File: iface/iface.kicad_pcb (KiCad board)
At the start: 2 copper layers, 215.9 x 152.4 mm, 157 parts, among them J1 Barrel_Jack_Switch, J10 4P4C, J11 4P4C, J12 4P4C, J2 Conn_01x16, J3 4P4C, J4 4P4C, J5 4P4C, J6 4P4C, J7 4P4C, J8 4P4C, J9 4P4C, Q1 BC847, Q10 BC847, Q11 BC847, Q12 BC847, Q13 BC847, Q14 BC847, Q15 BC847, Q16 BC847, Q17 BC847, Q18 BC847, Q19 BC847, Q2 BC847, Q20 BC847, Q21 BC847, Q22 BC847, Q23 BC847, Q24 BC847, Q25 BC847, Q26 BC847, Q27 BC847, Q28 BC847, Q29 BC847, Q3 BC847, Q30 BC847, Q31 BC847, Q32 BC847, Q33 BC847, Q34 BC847, Q35 BC847, Q36 BC847, Q37 BC847, Q38 BC847, Q39 BC847, Q4 BC847, Q40 BC847, Q5 BC847, Q6 BC847, Q7 BC847, Q8 BC847, Q9 BC847, SW1 SW_DPDT_x2, U1 74HC595, U10 PC817, U11 PC817, U12 PC817, U13 PC817, U14 PC817, U15 PC817, U16 PC817, U17 PC817, U18 PC817, U19 PC817, U2 74HC595, U20 PC817, U21 PC817, U22 PC817, U23 PC817, U24 PC817, U3 74HC04, U4 74HC04, U5 PC817, U6 PC817, U7 PC817, U8 PC817, U9 PC817

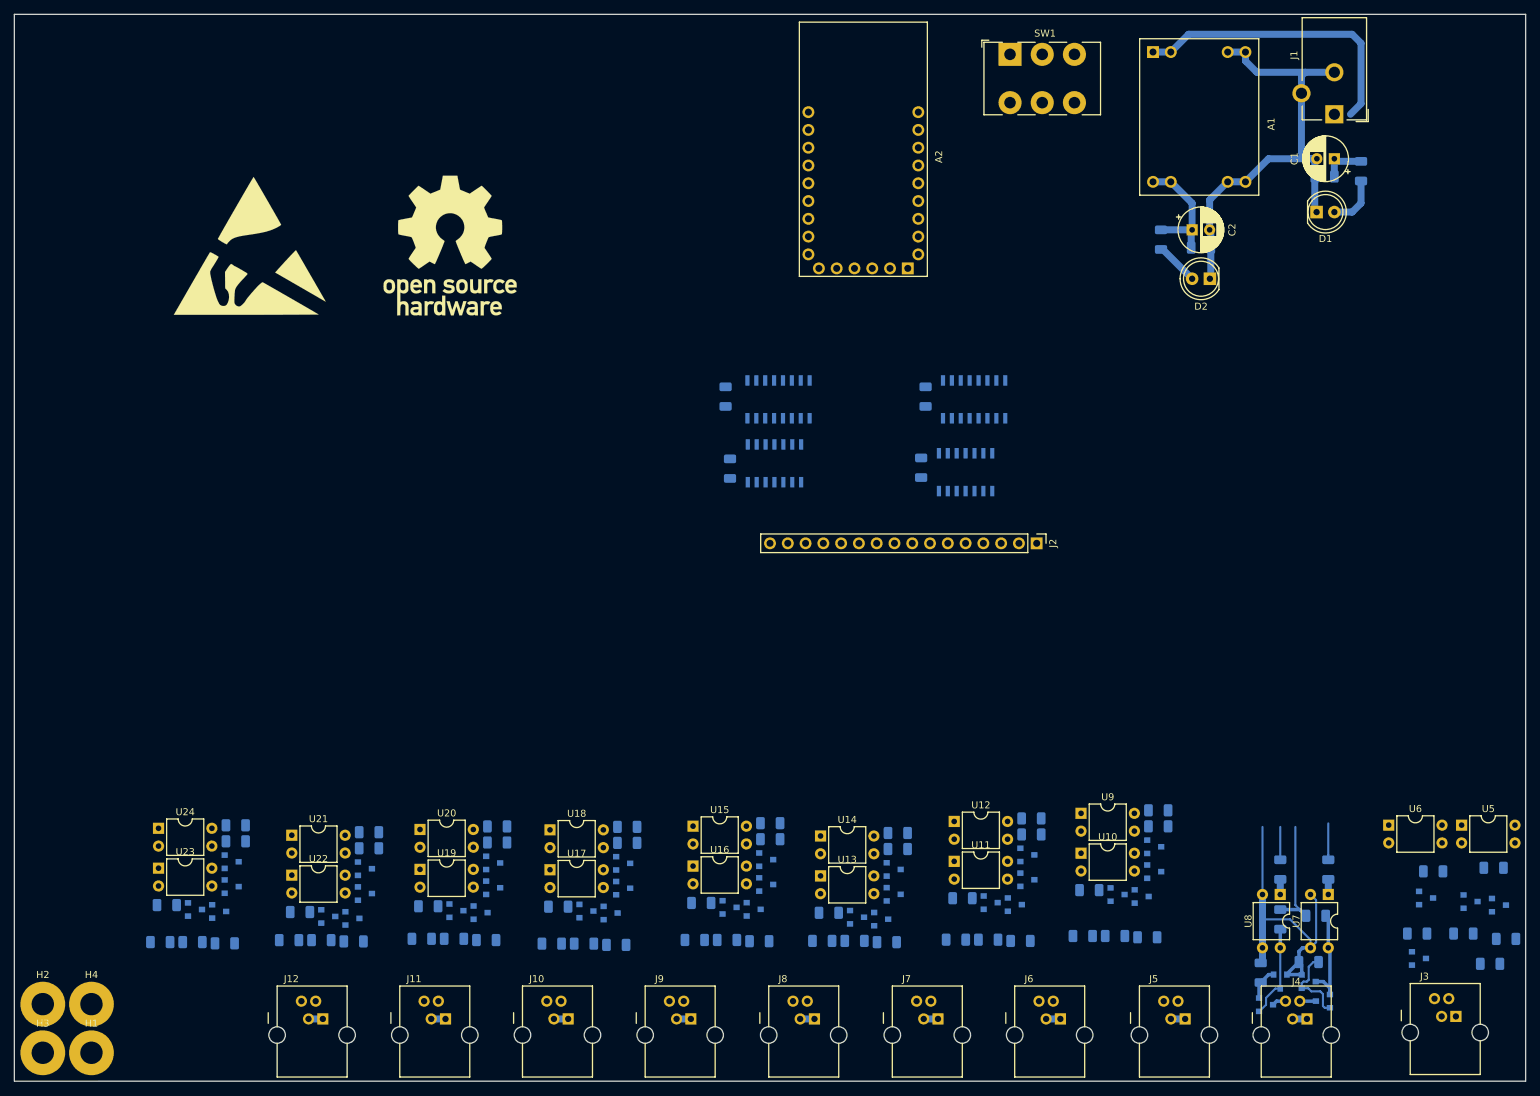
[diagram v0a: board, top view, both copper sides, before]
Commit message: iface: Finish routing the PCB layout
Signed-off-by: Sam Protsenko <joe.skb7@gmail.com>
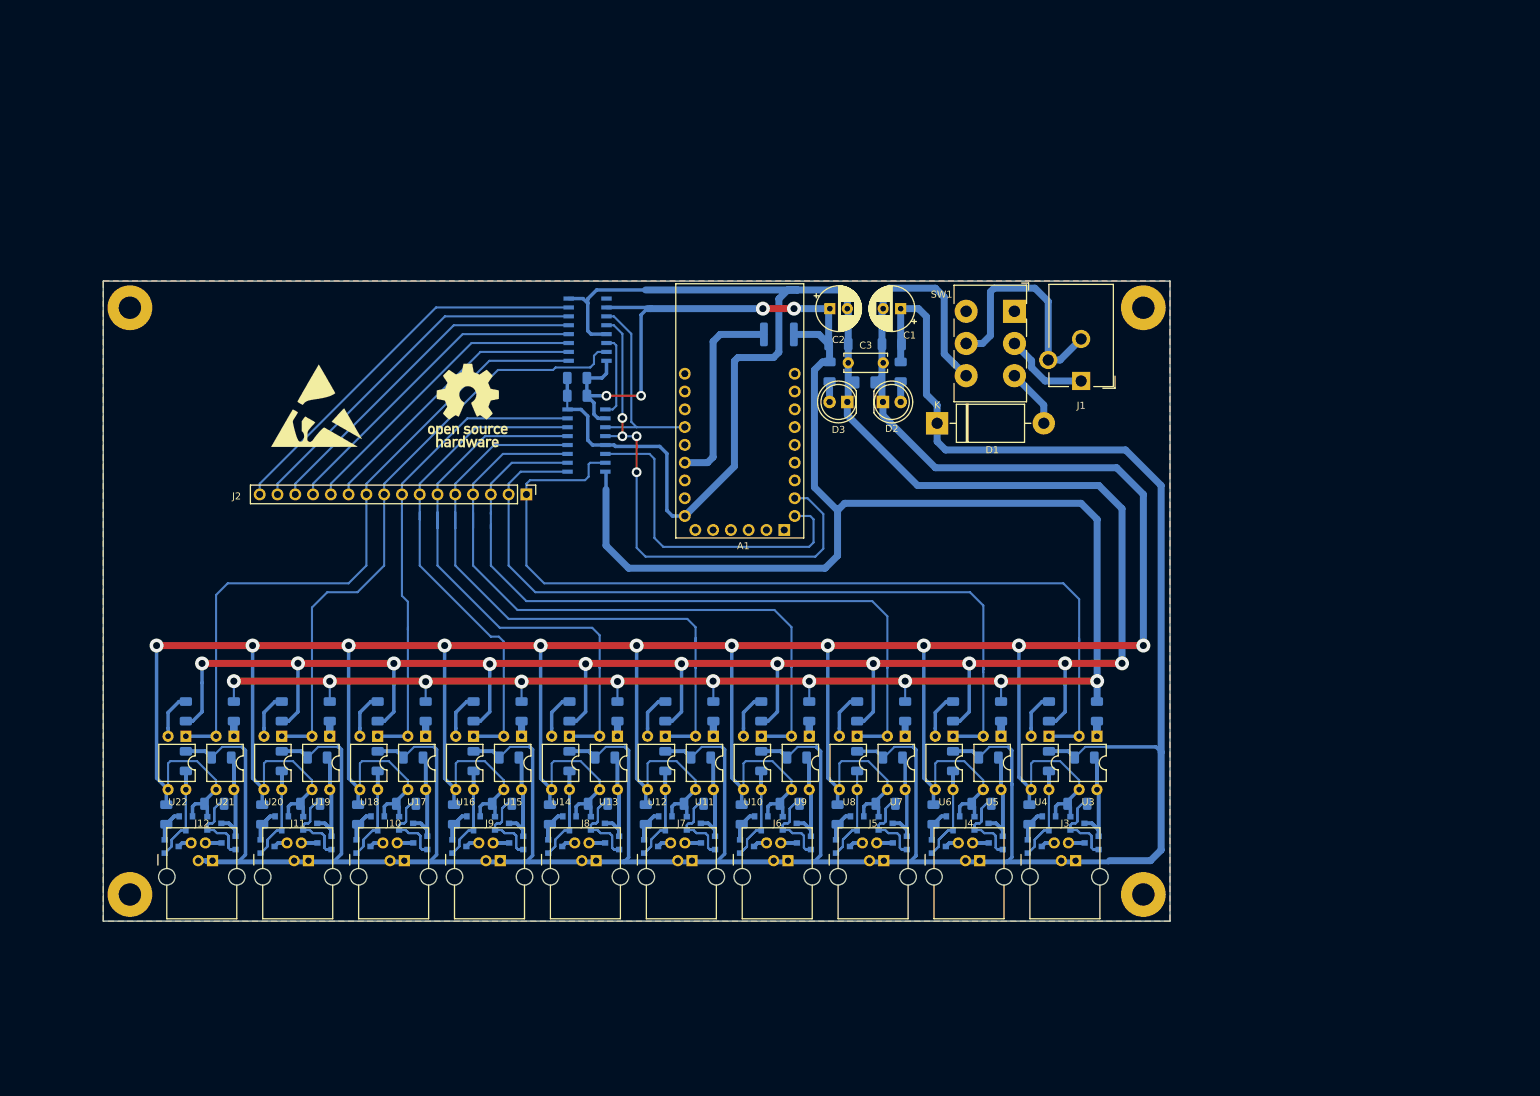
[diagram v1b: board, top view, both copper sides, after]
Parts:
- removed A2: FTDI232, Module_FTDI232:FTDI232
- removed the C4 at (233.0, 46.0)
- removed the C7 at (193.0, 77.5)
- removed C8: 100n, Capacitor_SMD:C_1206_3216Metric
- removed the D2 at (234.3, 50.5)
- removed U23, U24: PC817, Package_DIP:DIP-4_W7.62mm
- added C3: 1nF/2kV, Capacitor_THT:C_Disc_D6.0mm_W2.5mm_P5.00mm, F.Cu at (182.6, 62.5)
- added C6: 100nF, Capacitor_SMD:C_1206_3216Metric, B.Cu at (143.9, 64.6)
- added D1: 1N5822, Diode_THT:D_DO-201AD_P15.24mm_Horizontal, F.Cu at (195.3, 71.1)
- added D3: RED, LED_THT:LED_D5.0mm, F.Cu at (182.5, 68.1)
- added F1: Polyfuse, Fuse:Fuse_1812_4532Metric, B.Cu at (172.7, 58.4)
- added R63: 39R, Resistor_SMD:R_1206_3216Metric, B.Cu at (85.2, 127.0)
- A1: value MP1584_D-SUN -> FTDI232; footprint Module_MP1584:MP1584_D-SUN -> Module_FTDI232:FTDI232
- C1, C2: value 100uF x 25V -> 100uF/25V
- C4: renamed from C3; value 100n -> 100nF
- C5: value 100n -> 100nF
- C7: renamed from C6; value 100n -> 100nF
- R1: value 820R -> 1M
- R11, R17, R23, R29, R35, R41, R47, R5, R53, R59: value 10k -> 470R
- R13, R19, R25, R31, R37, R43, R49, R55, R61, R7: value 39R -> 10k
- R15, R21, R27, R33, R39, R45, R51, R57, R9: value 470R -> 39R
- R2: value 330R -> 820R
- R3: value 470R -> 330R
- SYM1: footprint Symbol:ESD-Logo_22x20mm_SilkScreen -> Symbol:ESD-Logo_13.2x12mm_SilkScreen
- SYM2: footprint Symbol:OSHW-Logo_19x20mm_SilkScreen -> Symbol:OSHW-Logo_11.4x12mm_SilkScreen
- U3, U4: value 74HC04 -> PC817; footprint Package_SO:SOIC-14_3.9x8.7mm_P1.27mm -> Package_DIP:DIP-4_W7.62mm; moved to F.Cu
- moved H2 186.1 mm to (224.8, 54.6)
- moved H3 158.8 mm to (224.8, 138.4)
- moved R3 126.1 mm to (180.0, 63.8), turned to 90 degrees
- moved H1 106.6 mm to (80.0, 54.6)
- moved A1 94.9 mm to (173.5, 86.4)
- moved R1 77.0 mm to (185.0, 65.3), turned to 0 degrees
- moved J2 73.2 mm to (136.7, 81.3)
- moved D2 67.6 mm to (187.6, 68.1)
- moved U5 67.0 mm to (204.5, 115.8), turned to 270 degrees
- moved C4 66.3 mm to (188.8, 59.8)
- moved C1 65.6 mm to (190.1, 54.7)
- moved Q2 65.3 mm to (211.3, 128.3), turned to 270 degrees
- moved R6 65.0 mm to (216.4, 118.9)
- moved U8 64.5 mm to (183.9, 115.8)
- moved U7 64.5 mm to (190.8, 115.8)
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- renumbered D1 to D2
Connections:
- net /Logic/G10 renamed /Logic/D10
- net /Logic/G11 renamed /Logic/D11
- net /Logic/G12 renamed /Logic/D12
- net /Logic/G13 renamed /Logic/D13
- net /Logic/G14 renamed /Logic/D14
- net /Logic/G15 renamed /Logic/D15
- A1 pad 1: +12V -> (no net)
- A1 pad 2: +12V -> (no net)
- A1 pad 3: GND -> (no net)
- A1 pad 4: GND -> (no net)
- A1 pad 5: +5V -> (no net)
- A1 pad 6: +5V -> (no net)
- A1 pad 7: GND -> GNDD
- A1 pad 8: GND -> (no net)
- C1 pad 2: GND -> GNDPWR
- C2 pad 2: GND -> GNDD
- C4 pad 2: GND -> GNDPWR
- C5 pad 2: GND -> GNDD
- C7 pad 2: GND -> GNDD
- D2 pad 1: GND -> GNDPWR
- D2 pad 2: Net-(D1-Pad2) -> Net-(D2-Pad2)
- H1 pad 1: GND -> GNDPWR
- H2 pad 1: GND -> GNDPWR
- H3 pad 1: GND -> GNDPWR
- H4 pad 1: GND -> GNDPWR
- J1 pad 2: GND -> Net-(J1-Pad2)
- J1 pad 3: GND -> Net-(J1-Pad2)
- J2 pad 1: /G0 -> /D0
- J2 pad 10: /G9 -> /D9
- J2 pad 2: /G1 -> /D1
- J2 pad 3: /G2 -> /D2
- J2 pad 4: /G3 -> /D3
- J2 pad 5: /G4 -> /D4
- J2 pad 6: /G5 -> /D5
- J2 pad 7: /G6 -> /D6
- J2 pad 8: /G7 -> /D7
- J2 pad 9: /G8 -> /D8
- Q1 pad 2: GND -> GNDPWR
- Q10 pad 2: GND -> GNDPWR
- Q13 pad 2: GND -> GNDPWR
- Q14 pad 2: GND -> GNDPWR
- Q17 pad 2: GND -> GNDPWR
- Q18 pad 2: GND -> GNDPWR
- Q2 pad 2: GND -> GNDPWR
- Q21 pad 2: GND -> GNDPWR
- Q22 pad 2: GND -> GNDPWR
- Q25 pad 2: GND -> GNDPWR
- Q26 pad 2: GND -> GNDPWR
- Q29 pad 2: GND -> GNDPWR
- Q30 pad 2: GND -> GNDPWR
- Q33 pad 2: GND -> GNDPWR
- Q34 pad 2: GND -> GNDPWR
- Q37 pad 2: GND -> GNDPWR
- Q38 pad 2: GND -> GNDPWR
- Q5 pad 2: GND -> GNDPWR
- Q6 pad 2: GND -> GNDPWR
- Q9 pad 2: GND -> GNDPWR
- R1 pad 1: Net-(D1-Pad2) -> GNDD
- R1 pad 2: +12V -> GNDPWR
- R10 pad 2: /G1 -> +5V
- R11 pad 1: +5V -> GNDD
- R11 pad 2: Net-(Q5-Pad3) -> Net-(R11-Pad2)
- R12 pad 1: +5V -> +12V
- R12 pad 2: Net-(Q6-Pad3) -> Net-(Q5-Pad3)
- R13 pad 1: Net-(Q5-Pad1) -> +12V
- R13 pad 2: GND -> Net-(Q6-Pad3)
- R14 pad 1: Net-(Q6-Pad1) -> Net-(Q5-Pad1)
- R14 pad 2: GND -> GNDPWR
- R15 pad 1: Net-(R15-Pad1) -> Net-(Q6-Pad1)
- R15 pad 2: /R2 -> GNDPWR
- R16 pad 2: /G2 -> +5V
- R17 pad 1: +5V -> GNDD
- R17 pad 2: Net-(Q11-Pad1) -> Net-(R17-Pad2)
- R18 pad 1: +5V -> +12V
- R18 pad 2: Net-(Q10-Pad3) -> Net-(Q11-Pad1)
- R19 pad 1: Net-(Q11-Pad2) -> +12V
- R19 pad 2: GND -> Net-(Q10-Pad3)
- R2 pad 2: +5V -> +12V
- R20 pad 1: Net-(Q10-Pad1) -> Net-(Q11-Pad2)
- R20 pad 2: GND -> GNDPWR
- R21 pad 1: Net-(R21-Pad1) -> Net-(Q10-Pad1)
- R21 pad 2: /R3 -> GNDPWR
- R22 pad 2: /G3 -> +5V
- R23 pad 1: +5V -> GNDD
- R23 pad 2: Net-(Q13-Pad3) -> Net-(R23-Pad2)
- R24 pad 1: +5V -> +12V
- R24 pad 2: Net-(Q14-Pad3) -> Net-(Q13-Pad3)
- R25 pad 1: Net-(Q13-Pad1) -> +12V
- R25 pad 2: GND -> Net-(Q14-Pad3)
- R26 pad 1: Net-(Q14-Pad1) -> Net-(Q13-Pad1)
- R26 pad 2: GND -> GNDPWR
- R27 pad 1: Net-(R27-Pad1) -> Net-(Q14-Pad1)
- R27 pad 2: /R4 -> GNDPWR
- R28 pad 2: /G4 -> +5V
- R29 pad 1: +5V -> GNDD
- R29 pad 2: Net-(Q17-Pad3) -> Net-(R29-Pad2)
- R3 pad 1: Net-(R3-Pad1) -> Net-(D3-Pad2)
- R3 pad 2: /R0 -> +5V
- R30 pad 1: +5V -> +12V
- R30 pad 2: Net-(Q18-Pad3) -> Net-(Q17-Pad3)
- R31 pad 1: Net-(Q17-Pad1) -> +12V
- R31 pad 2: GND -> Net-(Q18-Pad3)
- R32 pad 1: Net-(Q18-Pad1) -> Net-(Q17-Pad1)
- R32 pad 2: GND -> GNDPWR
- R33 pad 1: Net-(R33-Pad1) -> Net-(Q18-Pad1)
- R33 pad 2: /R5 -> GNDPWR
- R34 pad 2: /G5 -> +5V
- R35 pad 1: +5V -> GNDD
- R35 pad 2: Net-(Q21-Pad3) -> Net-(R35-Pad2)
- R36 pad 1: +5V -> +12V
- R36 pad 2: Net-(Q22-Pad3) -> Net-(Q21-Pad3)
- R37 pad 1: Net-(Q21-Pad1) -> +12V
- R37 pad 2: GND -> Net-(Q22-Pad3)
- R38 pad 1: Net-(Q22-Pad1) -> Net-(Q21-Pad1)
- R38 pad 2: GND -> GNDPWR
- R39 pad 1: Net-(R39-Pad1) -> Net-(Q22-Pad1)
- R39 pad 2: /R6 -> GNDPWR
- R4 pad 2: /G0 -> +5V
- R40 pad 2: /G6 -> +5V
- R41 pad 1: +5V -> GNDD
- R41 pad 2: Net-(Q25-Pad3) -> Net-(R41-Pad2)
- R42 pad 1: +5V -> +12V
- R42 pad 2: Net-(Q26-Pad3) -> Net-(Q25-Pad3)
- R43 pad 1: Net-(Q25-Pad1) -> +12V
- R43 pad 2: GND -> Net-(Q26-Pad3)
- R44 pad 1: Net-(Q26-Pad1) -> Net-(Q25-Pad1)
- R44 pad 2: GND -> GNDPWR
- R45 pad 1: Net-(R45-Pad1) -> Net-(Q26-Pad1)
- R45 pad 2: /R7 -> GNDPWR
- R46 pad 2: /G7 -> +5V
- R47 pad 1: +5V -> GNDD
- R47 pad 2: Net-(Q29-Pad3) -> Net-(R47-Pad2)
- R48 pad 1: +5V -> +12V
- R48 pad 2: Net-(Q30-Pad3) -> Net-(Q29-Pad3)
- R49 pad 1: Net-(Q29-Pad1) -> +12V
- R49 pad 2: GND -> Net-(Q30-Pad3)
- R5 pad 1: +5V -> GNDD
- R5 pad 2: Net-(Q1-Pad3) -> Net-(R5-Pad2)
- R50 pad 1: Net-(Q30-Pad1) -> Net-(Q29-Pad1)
- R50 pad 2: GND -> GNDPWR
- R51 pad 1: Net-(R51-Pad1) -> Net-(Q30-Pad1)
- R51 pad 2: /R8 -> GNDPWR
- R52 pad 2: /G8 -> +5V
- R53 pad 1: +5V -> GNDD
- R53 pad 2: Net-(Q33-Pad3) -> Net-(R53-Pad2)
- R54 pad 1: +5V -> +12V
- R54 pad 2: Net-(Q34-Pad3) -> Net-(Q33-Pad3)
- R55 pad 1: Net-(Q33-Pad1) -> +12V
- R55 pad 2: GND -> Net-(Q34-Pad3)
- R56 pad 1: Net-(Q34-Pad1) -> Net-(Q33-Pad1)
- R56 pad 2: GND -> GNDPWR
- R57 pad 1: Net-(R57-Pad1) -> Net-(Q34-Pad1)
- R57 pad 2: /R9 -> GNDPWR
- R58 pad 2: /G9 -> +5V
- R59 pad 1: +5V -> GNDD
- R59 pad 2: Net-(Q37-Pad3) -> Net-(R59-Pad2)
- R6 pad 1: +5V -> +12V
- R6 pad 2: Net-(Q2-Pad3) -> Net-(Q1-Pad3)
- R60 pad 1: +5V -> +12V
- R60 pad 2: Net-(Q38-Pad3) -> Net-(Q37-Pad3)
- R61 pad 1: Net-(Q37-Pad1) -> +12V
- R61 pad 2: GND -> Net-(Q38-Pad3)
- R62 pad 1: Net-(Q38-Pad1) -> Net-(Q37-Pad1)
- R62 pad 2: GND -> GNDPWR
- R7 pad 1: Net-(Q1-Pad1) -> +12V
- R7 pad 2: GND -> Net-(Q2-Pad3)
- R8 pad 1: Net-(Q2-Pad1) -> Net-(Q1-Pad1)
- R8 pad 2: GND -> GNDPWR
- R9 pad 1: Net-(R9-Pad1) -> Net-(Q2-Pad1)
- R9 pad 2: /R1 -> GNDPWR
- SW1 pad 3: +12V -> Net-(D1-Pad2)
- SW1 pad 5: (no net) -> Net-(J1-Pad2)
- SW1 pad 6: (no net) -> GNDPWR
- U1 pad 1: /G1 -> /D1
- U1 pad 13: GND -> GNDD
- U1 pad 15: /G0 -> /D0
- U1 pad 2: /G2 -> /D2
- U1 pad 3: /G3 -> /D3
- U1 pad 4: /G4 -> /D4
- U1 pad 5: /G5 -> /D5
- U1 pad 6: /G6 -> /D6
- U1 pad 7: /G7 -> /D7
- U1 pad 8: GND -> GNDD
- U10 pad 1: Net-(R16-Pad1) -> /D3
- U10 pad 2: GND -> Net-(R23-Pad2)
- U10 pad 3: GND -> GNDPWR
- U10 pad 4: Net-(Q10-Pad3) -> Net-(Q14-Pad3)
- U11 pad 1: Net-(R21-Pad1) -> Net-(R28-Pad1)
- U11 pad 2: GND -> /D4
- U11 pad 3: GND -> GNDPWR
- U11 pad 4: Net-(Q13-Pad3) -> Net-(Q17-Pad3)
- U12 pad 1: Net-(R22-Pad1) -> /D4
- U12 pad 2: GND -> Net-(R29-Pad2)
- U12 pad 3: GND -> GNDPWR
- U12 pad 4: Net-(Q14-Pad3) -> Net-(Q18-Pad3)
- U13 pad 1: Net-(R27-Pad1) -> Net-(R34-Pad1)
- U13 pad 2: GND -> /D5
- U13 pad 3: GND -> GNDPWR
- U13 pad 4: Net-(Q17-Pad3) -> Net-(Q21-Pad3)
- U14 pad 1: Net-(R28-Pad1) -> /D5
- U14 pad 2: GND -> Net-(R35-Pad2)
- U14 pad 3: GND -> GNDPWR
- U14 pad 4: Net-(Q18-Pad3) -> Net-(Q22-Pad3)
- U15 pad 1: Net-(R33-Pad1) -> Net-(R40-Pad1)
- U15 pad 2: GND -> /D6
- U15 pad 3: GND -> GNDPWR
- U15 pad 4: Net-(Q21-Pad3) -> Net-(Q25-Pad3)
- U16 pad 1: Net-(R34-Pad1) -> /D6
- U16 pad 2: GND -> Net-(R41-Pad2)
- U16 pad 3: GND -> GNDPWR
- U16 pad 4: Net-(Q22-Pad3) -> Net-(Q26-Pad3)
- U17 pad 1: Net-(R39-Pad1) -> Net-(R46-Pad1)
- U17 pad 2: GND -> /D7
- U17 pad 3: GND -> GNDPWR
- U17 pad 4: Net-(Q25-Pad3) -> Net-(Q29-Pad3)
- U18 pad 1: Net-(R40-Pad1) -> /D7
- U18 pad 2: GND -> Net-(R47-Pad2)
- U18 pad 3: GND -> GNDPWR
- U18 pad 4: Net-(Q26-Pad3) -> Net-(Q30-Pad3)
- U19 pad 1: Net-(R45-Pad1) -> Net-(R52-Pad1)
- U19 pad 2: GND -> /D8
- U19 pad 3: GND -> GNDPWR
- U19 pad 4: Net-(Q29-Pad3) -> Net-(Q33-Pad3)
- U2 pad 1: /G9 -> /D9
- U2 pad 13: GND -> GNDD
- U2 pad 15: /G8 -> /D8
- U2 pad 8: GND -> GNDD
- U20 pad 1: Net-(R46-Pad1) -> /D8
- U20 pad 2: GND -> Net-(R53-Pad2)
- U20 pad 3: GND -> GNDPWR
- U20 pad 4: Net-(Q30-Pad3) -> Net-(Q34-Pad3)
- U21 pad 1: Net-(R51-Pad1) -> Net-(R58-Pad1)
- U21 pad 2: GND -> /D9
- U21 pad 3: GND -> GNDPWR
- U21 pad 4: Net-(Q33-Pad3) -> Net-(Q37-Pad3)
- U22 pad 1: Net-(R52-Pad1) -> /D9
- U22 pad 2: GND -> Net-(R59-Pad2)
- U22 pad 3: GND -> GNDPWR
- U22 pad 4: Net-(Q34-Pad3) -> Net-(Q38-Pad3)
- U3 pad 1: /G0 -> Net-(R4-Pad1)
- U3 pad 2: /R0 -> /D0
- U3 pad 3: /G1 -> GNDPWR
- U3 pad 4: /R1 -> Net-(Q1-Pad3)
- U4 pad 1: /G6 -> /D0
- U4 pad 2: /R6 -> Net-(R5-Pad2)
- U4 pad 3: /G7 -> GNDPWR
- U4 pad 4: /R7 -> Net-(Q2-Pad3)
- U5 pad 1: Net-(R3-Pad1) -> Net-(R10-Pad1)
- U5 pad 2: GND -> /D1
- U5 pad 3: GND -> GNDPWR
- U5 pad 4: Net-(Q1-Pad3) -> Net-(Q5-Pad3)
- U6 pad 1: Net-(R4-Pad1) -> /D1
- U6 pad 2: GND -> Net-(R11-Pad2)
- U6 pad 3: GND -> GNDPWR
- U6 pad 4: Net-(Q2-Pad3) -> Net-(Q6-Pad3)
- U7 pad 1: Net-(R9-Pad1) -> Net-(R16-Pad1)
- U7 pad 2: GND -> /D2
- U7 pad 3: GND -> GNDPWR
- U7 pad 4: Net-(Q5-Pad3) -> Net-(Q11-Pad1)
- U8 pad 1: Net-(R10-Pad1) -> /D2
- U8 pad 2: GND -> Net-(R17-Pad2)
- U8 pad 3: GND -> GNDPWR
- U8 pad 4: Net-(Q6-Pad3) -> Net-(Q10-Pad3)
- U9 pad 1: Net-(R15-Pad1) -> Net-(R22-Pad1)
- U9 pad 2: GND -> /D3
- U9 pad 3: GND -> GNDPWR
- U9 pad 4: Net-(Q11-Pad1) -> Net-(Q13-Pad3)
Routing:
- net GNDPWR: track 0.00 -> 694.9 mm, vias 0 -> 11
- net +12V: track 66.9 -> 577.8 mm
- net GNDD: track 0.00 -> 442.1 mm, vias 0 -> 11
- net +5V: track 36.0 -> 370.2 mm, vias 0 -> 14
- net /D0: track 0.00 -> 130.5 mm
- net GND: track 116.6 -> 0.00 mm
- net /D1: track 0.00 -> 114.4 mm
- net /D2: track 0.00 -> 105.9 mm
- net /D3: track 0.00 -> 98.5 mm
- net /D9: track 0.00 -> 95.6 mm
- net /D4: track 0.00 -> 90.8 mm
- net /D8: track 0.00 -> 87.5 mm
- net /D5: track 0.00 -> 81.8 mm
- net /Logic/LATCH: track 0.00 -> 75.6 mm, vias 0 -> 4
- net /D6: track 0.00 -> 71.5 mm
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- added copper zone on B.Cu, net GNDPWR
- added copper zone on F.Cu, net GNDPWR
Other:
- board size 215.9 x 152.4 mm -> 152.4 x 91.4 mm
- net class Default: clearance 0.3 -> 0.4; via_dia 1.2 -> 1.4
- rule trace_clearance: 0.3 -> 0.4
- rule via_min_size: 1.2 -> 1.4

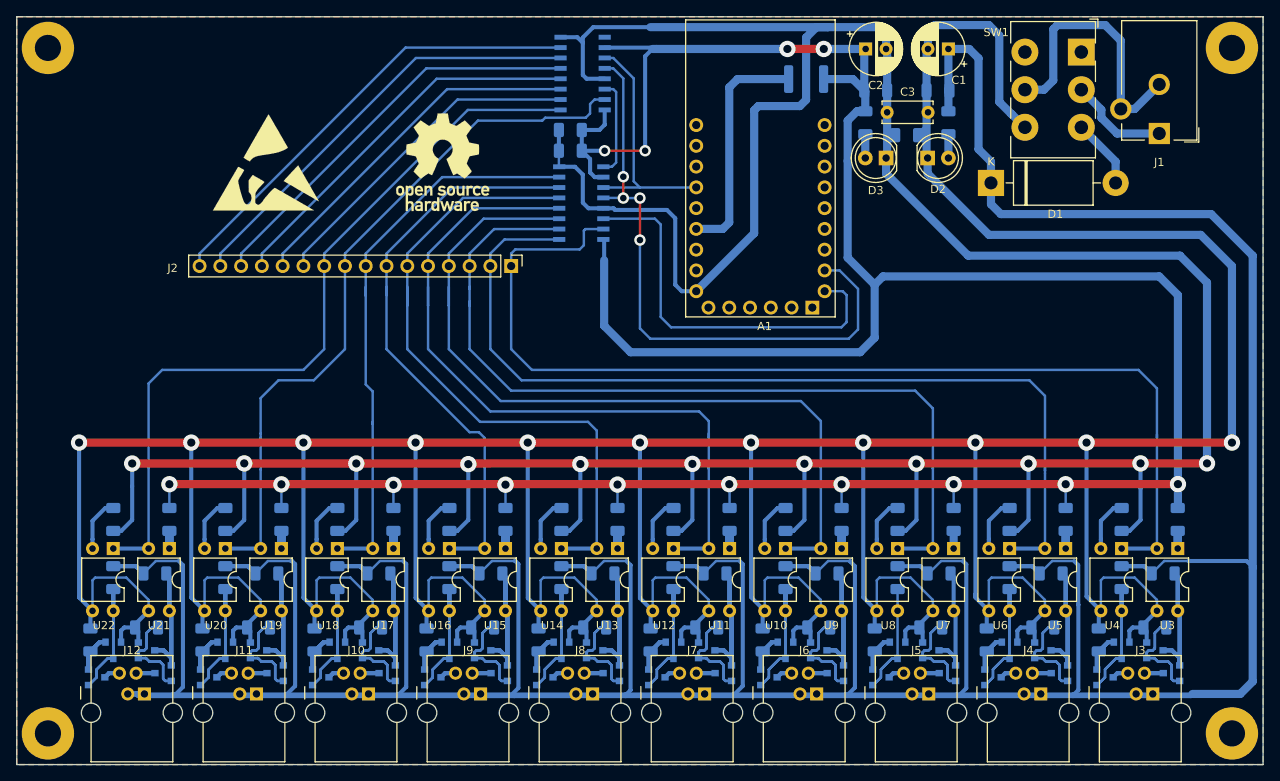
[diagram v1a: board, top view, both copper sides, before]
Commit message: iface: Update PCB for toner transfer method
Signed-off-by: Sam Protsenko <joe.skb7@gmail.com>
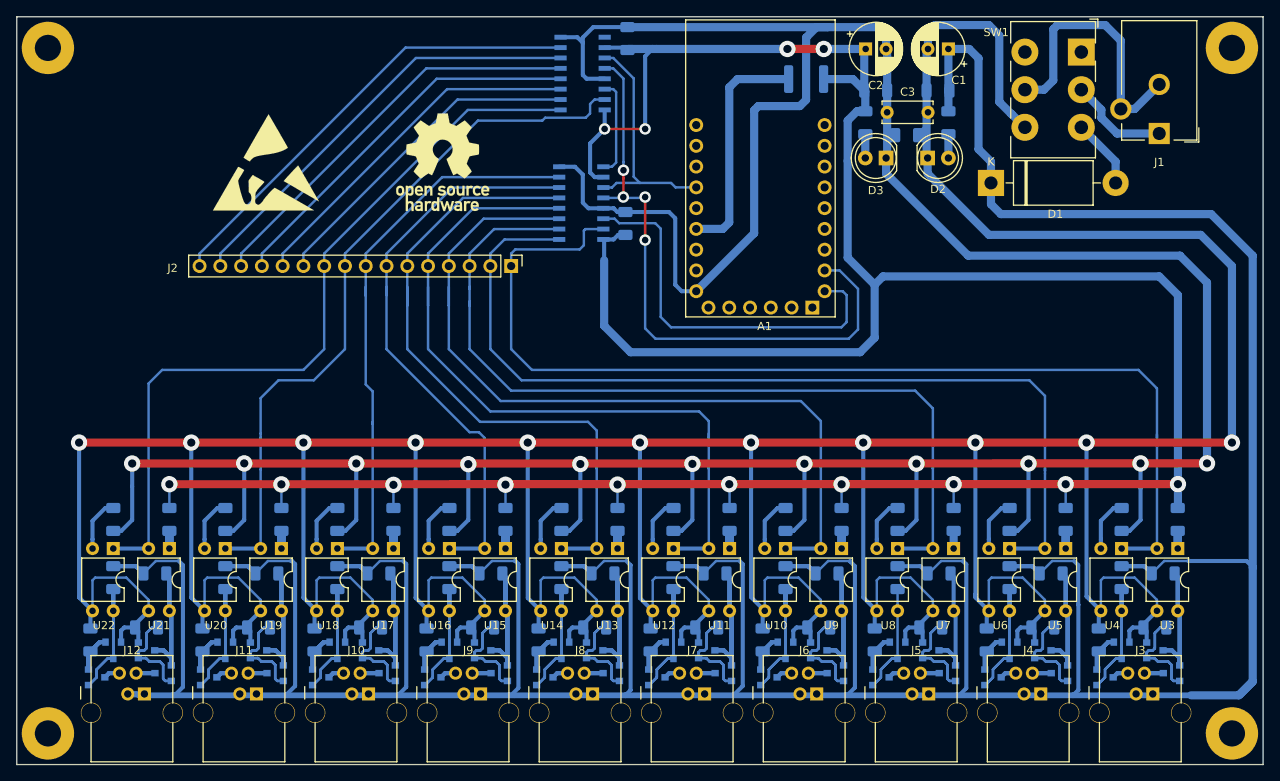
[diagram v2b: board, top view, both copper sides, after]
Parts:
- moved C6 13.2 mm to (150.9, 53.5), turned to 90 degrees
- moved C7 11.2 mm to (150.6, 76.1), turned to 90 degrees
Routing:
- net +5V: track 370.2 -> 363.5 mm
- net +12V: track 577.8 -> 582.4 mm
- net GNDD: track 442.1 -> 437.6 mm
- removed copper zone on B.Cu, net GNDPWR
- removed copper zone on F.Cu, net GNDPWR
